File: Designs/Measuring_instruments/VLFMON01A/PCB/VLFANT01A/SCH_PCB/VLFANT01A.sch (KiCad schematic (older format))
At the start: 13 parts, among them J1 CONN_3, J2 CONN_3, J3 CONN_3, J4 CONN_3, J5 CONN_3, J6 CONN_3, J7 SMA, J8 CONN_3, J9 JUMP_3X2, M1 HOLE, M2 HOLE, M3 HOLE, M4 HOLE

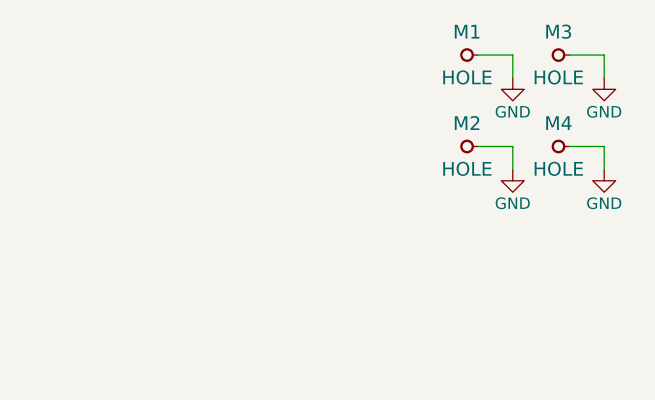
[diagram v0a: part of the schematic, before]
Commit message: 
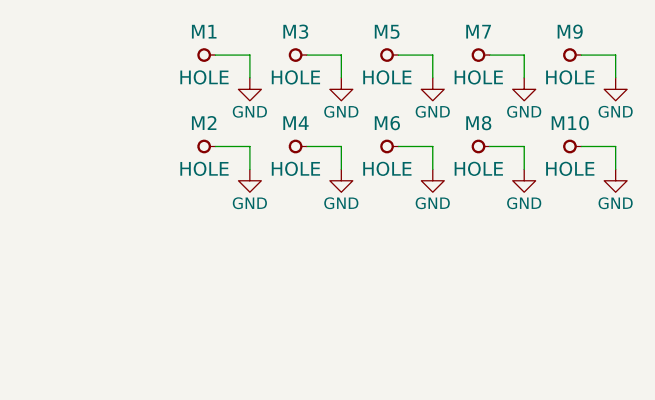
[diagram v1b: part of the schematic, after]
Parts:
- added M10, M5, M6, M7, M8, M9: HOLE, Mlab_Mechanical:MountingHole_3mm, symbol HOLE
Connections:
- net GND: now also M10.1, M5.1, M6.1, M7.1, M8.1, M9.1
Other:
- moved on the sheet: M1, M2, M3, M4
